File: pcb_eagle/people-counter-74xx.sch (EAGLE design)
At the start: 66 parts, among them IC1 74LS90N, IC2 74LS90N, IC3 74LS90N, IC4 74LS90N, IC5 74LS47N, IC6 74LS47N, IC7 74LS47N, IC8 74LS47N, IC9 NE555N, X1 USB-MICRO-B-BOTTOM

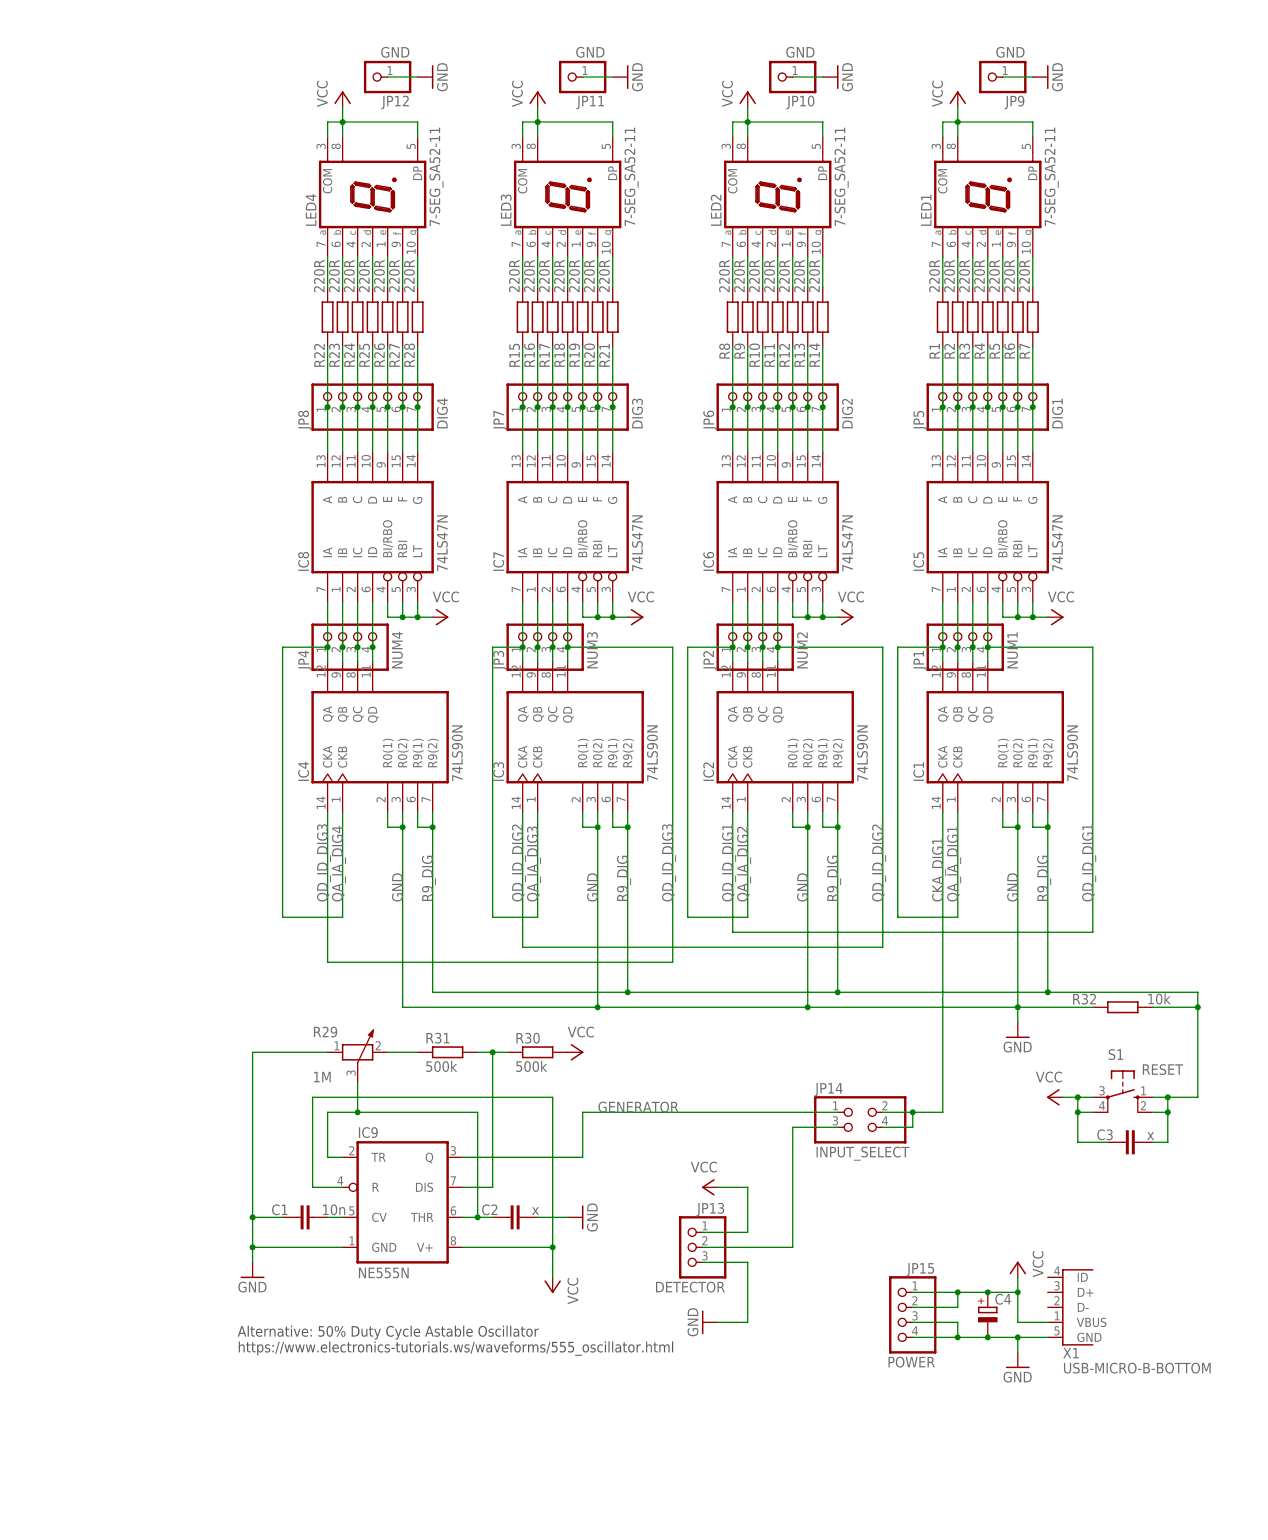
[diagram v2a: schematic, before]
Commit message: PCB_EAGLE: final layout of board
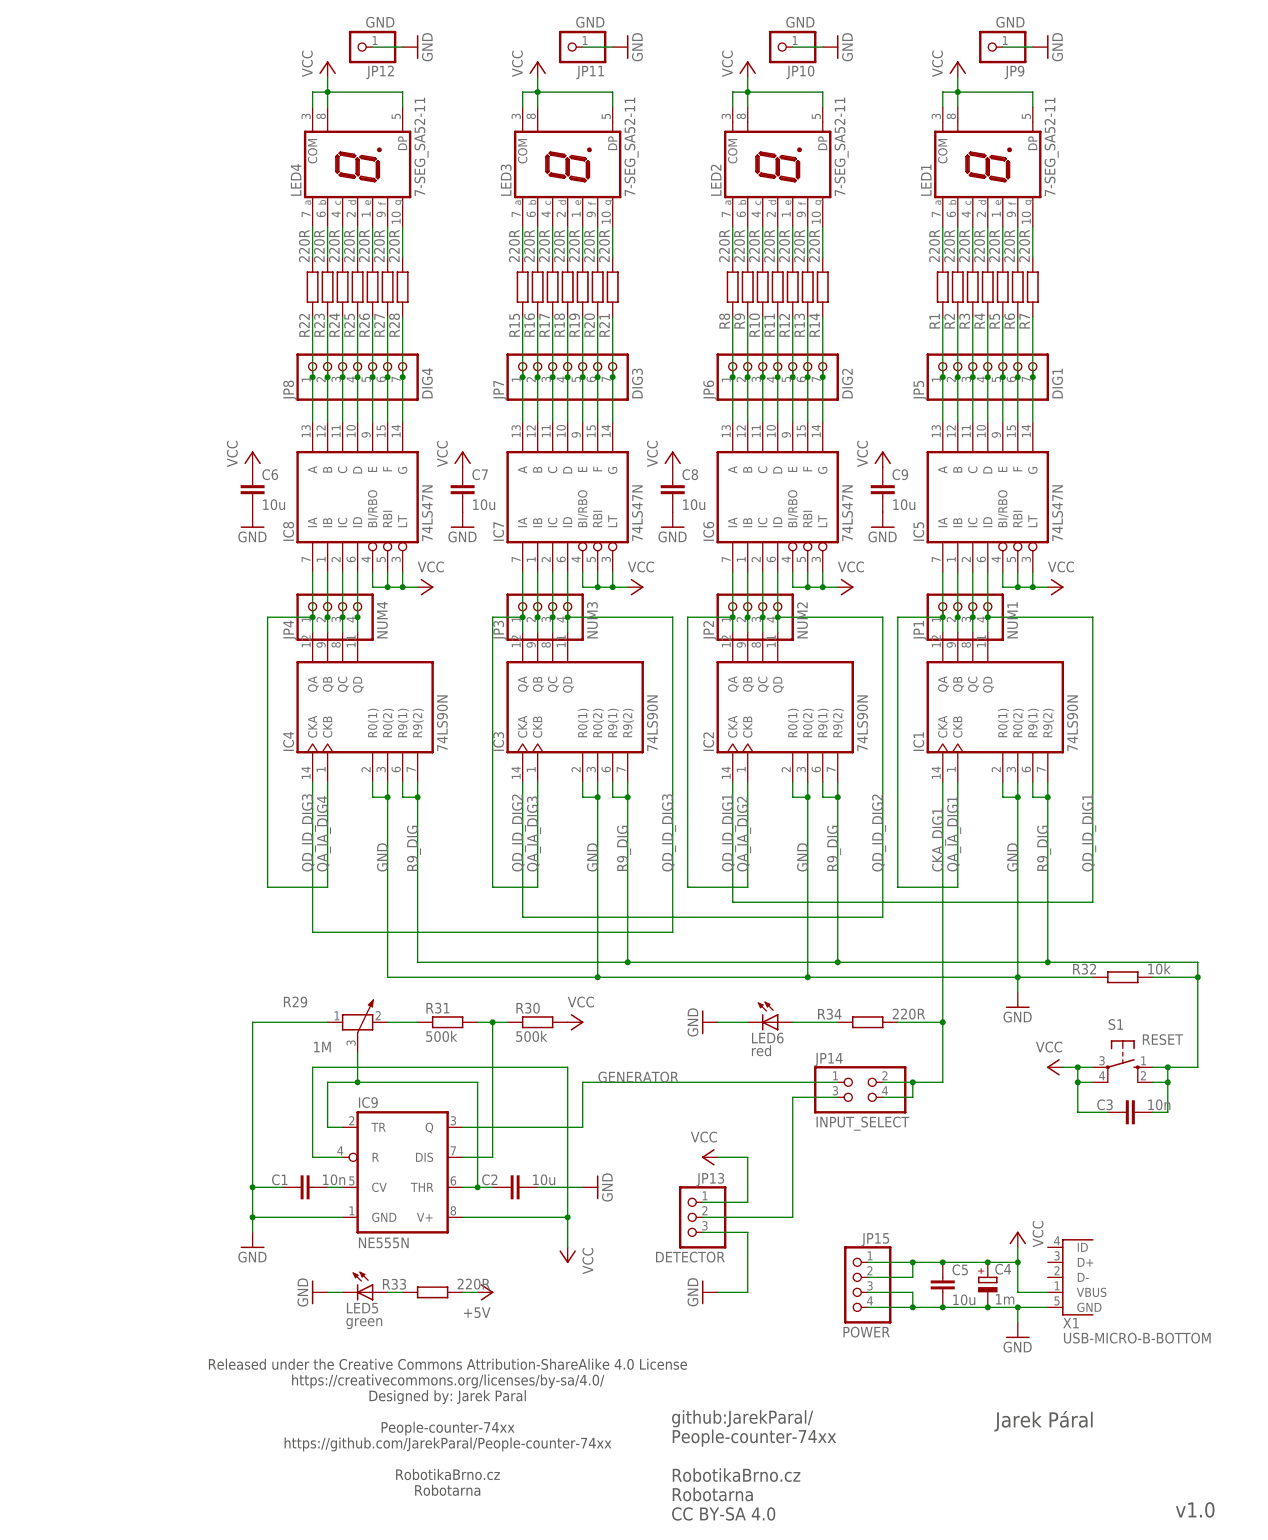
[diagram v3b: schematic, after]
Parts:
- added C5, C6, C7, C8, C9: 10u, rcl:C-EUC0805
- added LED5: green, led:LEDCHIPLED_0603
- added LED6: red, led:LEDCHIPLED_0603
- added R33, R34: 220R, rcl:R-EU_R0603
- C2: value x -> 10u; device rcl:C-EUC0603 -> rcl:C-EUC0805
- C3: value x -> 10n
- C4: value (none) -> 1m
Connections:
- new net +5V: R33.2
- new net N$1: LED6.A, R34.1
- new net N$11: LED5.A, R33.1
- net CKA_DIG1: now also R34.2
- net GND: now also C5.2, C6.2, C7.2, C8.2, C9.2, LED5.C, LED6.C
- net VCC: now also C5.1, C6.1, C7.1, C8.1, C9.1
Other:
- note added: "Jarek Páral"
- note added: "Released under the Creative Commons Attribution-ShareAlike 4.0 License https://creativecommons.org/licenses/by-sa/4.0/ Designed by: Jarek Paral People-counter-74xx https://github.com/JarekParal/People-counter-74xx RobotikaBrno.cz Robotarna"
- note added: "github:JarekParal/ People-counter-74xx RobotikaBrno.cz Robotarna CC BY-SA 4.0"
- note added: "v1.0"
- note removed: "Alternative: 50% Duty Cycle Astable Oscillator https://www.electronics-tutorials.ws/waveforms/555_oscillator.html"
- moved on the sheet: C1, C2, C3, C4, IC1, IC2, IC3, IC4, IC5, IC6, IC7, IC8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

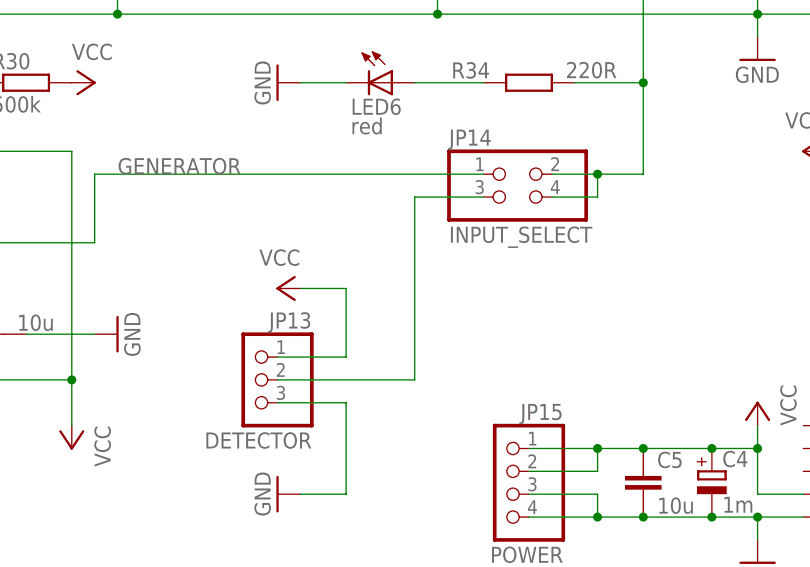
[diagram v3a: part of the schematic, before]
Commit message: PCB_EAGLE: add a few description text and some optimization of net
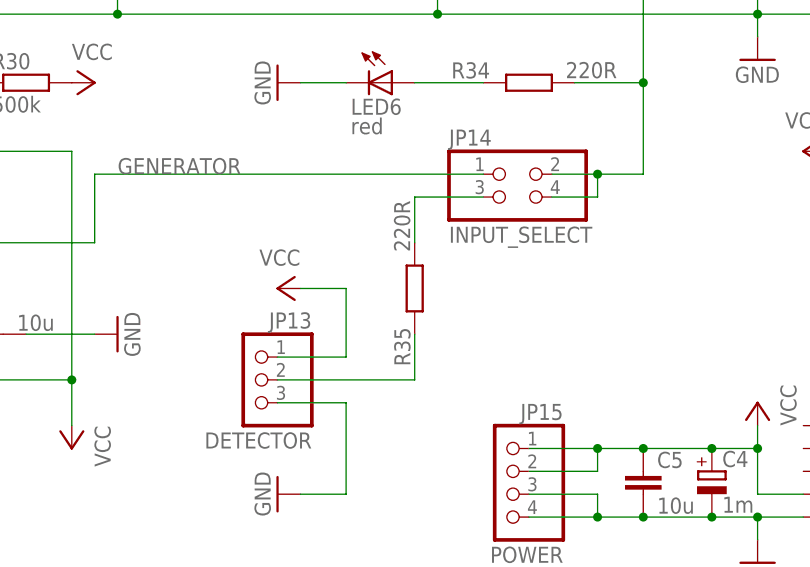
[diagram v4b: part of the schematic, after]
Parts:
- added R35: 220R, rcl:R-EU_R0603
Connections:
- removed net N$5: JP13.2, JP14.3
- new net SIGNAL_INPUT: JP13.2, R35.1
- new net SIGNAL_INPUT_: JP14.3, R35.2
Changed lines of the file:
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@@
 <part name="GND15" library="supply1" deviceset="GND" device=""/>
 <part name="R34" library="rcl" library_urn="urn:adsk.eagle:library:334" deviceset="R-EU_" device="R0603" package3d_urn="urn:adsk.eagle:package:23555/2" value="220R"/>
+<part name="R35" library="rcl" library_urn="urn:adsk.eagle:library:334" deviceset="R-EU_" device="R0603" package3d_urn="urn:adsk.eagle:package:23555/2" value="220R"/>
 </parts>
 <sheets>
@@
 <attribute name="VALUE" x="100.584" y="-73.152" size="1.778" layer="96"/>
 </instance>
+<instance part="R35" gate="G$1" x="83.82" y="-96.52" smashed="yes" rot="R90">
+<attribute name="NAME" x="83.3374" y="-100.838" size="1.778" layer="95" rot="MR270"/>
+<attribute name="VALUE" x="83.312" y="-92.456" size="1.778" layer="96" rot="R90"/>
+</instance>
 </instances>
 <busses>
@@
 </segment>
 </net>
-<net name="N$5" class="0">
+<net name="SIGNAL_INPUT" class="0">
 <segment>
 <pinref part="JP13" gate="A" pin="2"/>
 <wire x1="68.58" y1="-106.68" x2="83.82" y2="-106.68" width="0.1524" layer="91"/>
-<wire x1="83.82" y1="-106.68" x2="83.82" y2="-86.36" width="0.1524" layer="91"/>
-<pinref part="JP14" gate="A" pin="3"/>
-<wire x1="83.82" y1="-86.36" x2="91.44" y2="-86.36" width="0.1524" layer="91"/>
+<pinref part="R35" gate="G$1" pin="1"/>
+<wire x1="83.82" y1="-101.6" x2="83.82" y2="-106.68" width="0.1524" layer="91"/>
 </segment>
 </net>
@@
 </segment>
 </net>
+<net name="SIGNAL_INPUT_" class="0">
+<segment>
+<pinref part="JP14" gate="A" pin="3"/>
+<wire x1="83.82" y1="-86.36" x2="91.44" y2="-86.36" width="0.1524" layer="91"/>
+<pinref part="R35" gate="G$1" pin="2"/>
+<wire x1="83.82" y1="-91.44" x2="83.82" y2="-86.36" width="0.1524" layer="91"/>
+</segment>
+</net>

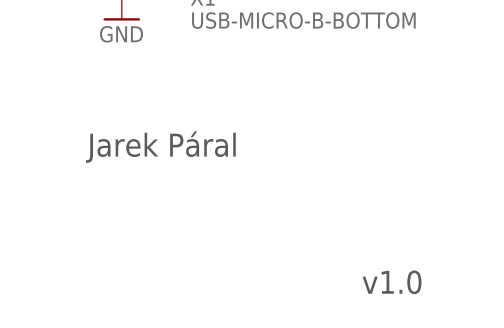
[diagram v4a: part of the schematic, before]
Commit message: PCB_EAGLE: start work on version 1.1 - repair layer of texts Robotarna RobotikaBrno
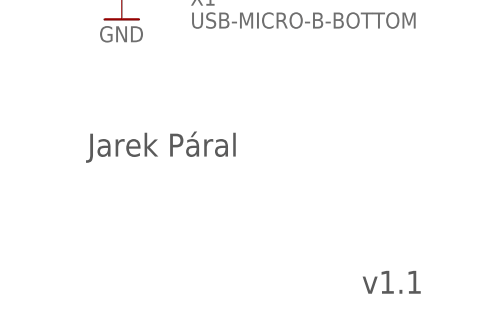
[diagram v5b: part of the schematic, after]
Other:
- note added: "v1.1"
- note removed: "v1.0"
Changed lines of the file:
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@@
 CC BY-SA 4.0</text>
 <text x="118.11" y="-142.24" size="2.54" layer="97" font="vector" ratio="14">Jarek Páral</text>
-<text x="148.59" y="-157.48" size="2.54" layer="97" font="vector" ratio="14">v1.0</text>
+<text x="148.59" y="-157.48" size="2.54" layer="97" font="vector" ratio="14">v1.1</text>
 <rectangle x1="511.290040625" y1="-62.8899625" x2="511.503396875" y2="-62.8798" layer="102"/>
 <rectangle x1="511.1478" y1="-62.8798" x2="511.6456375" y2="-62.86964375" layer="102"/>

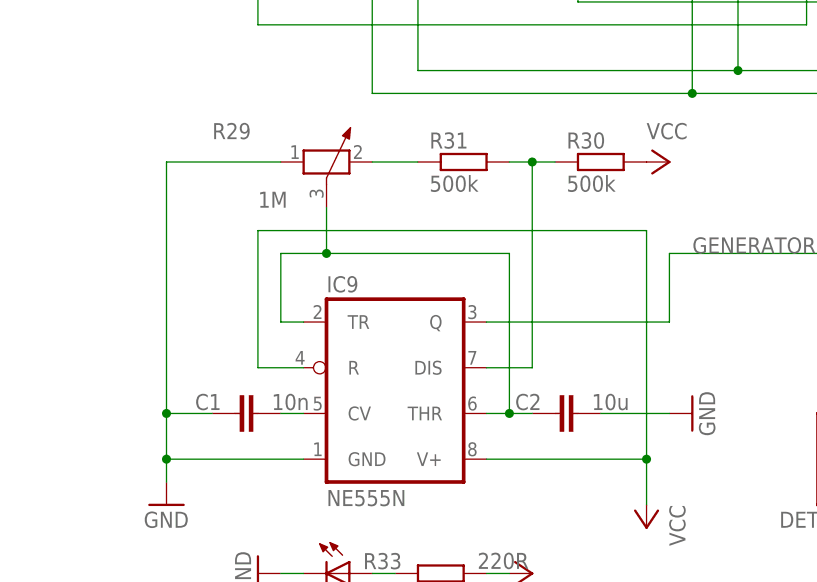
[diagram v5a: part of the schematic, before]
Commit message: PCB_EAGLE: fix two bugs from v1.0 - change value of C2 (10u -> 200n) - delete one wire on potentiometer (R29)
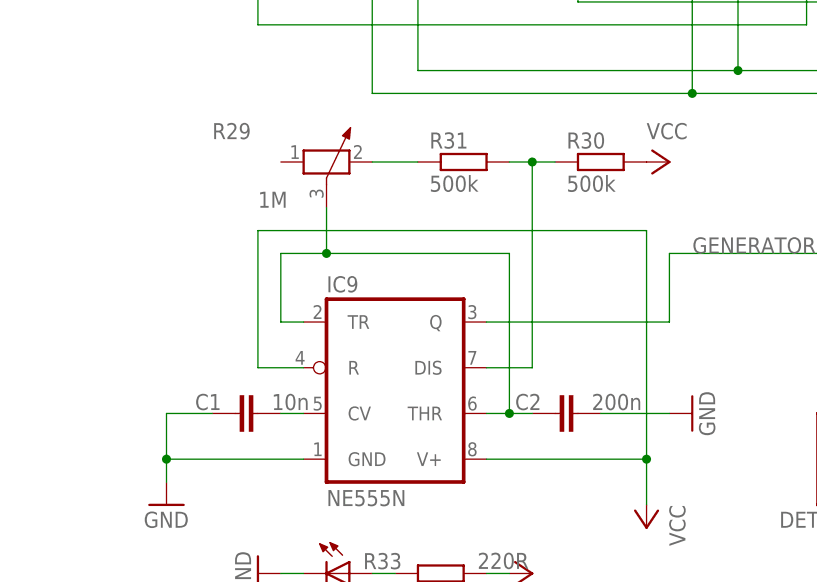
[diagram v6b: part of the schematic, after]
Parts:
- C2: value 10u -> 200n
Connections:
- net GND: no longer R29.1
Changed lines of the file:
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@@
 <?xml version="1.0" encoding="utf-8"?>
 <!DOCTYPE eagle SYSTEM "eagle.dtd">
-<eagle version="8.6.0">
+<eagle version="9.1.2">
 <drawing>
 <settings>
@@
 <part name="JP13" library="pinhead" library_urn="urn:adsk.eagle:library:325" deviceset="PINHD-1X3" device="/90" package3d_urn="urn:adsk.eagle:package:22459/2" value="DETECTOR"/>
 <part name="R32" library="rcl" library_urn="urn:adsk.eagle:library:334" deviceset="R-EU_" device="R0603" package3d_urn="urn:adsk.eagle:package:23555/2" value="10k"/>
-<part name="C2" library="rcl" library_urn="urn:adsk.eagle:library:334" deviceset="C-EU" device="C0805" package3d_urn="urn:adsk.eagle:package:23617/2" value="10u"/>
+<part name="C2" library="rcl" library_urn="urn:adsk.eagle:library:334" deviceset="C-EU" device="C0805" package3d_urn="urn:adsk.eagle:package:23617/2" value="200n"/>
 <part name="C3" library="rcl" library_urn="urn:adsk.eagle:library:334" deviceset="C-EU" device="C0603" package3d_urn="urn:adsk.eagle:package:23616/2" value="10n"/>
 <part name="GND1" library="supply1" library_urn="urn:adsk.eagle:library:371" deviceset="GND" device=""/>
@@
 <pinref part="C1" gate="G$1" pin="1"/>
 <wire x1="-7.62" y1="-101.6" x2="-2.54" y2="-101.6" width="0.1524" layer="91"/>
-<pinref part="R29" gate="1" pin="1"/>
-<wire x1="5.08" y1="-73.66" x2="-7.62" y2="-73.66" width="0.1524" layer="91"/>
-<wire x1="-7.62" y1="-73.66" x2="-7.62" y2="-101.6" width="0.1524" layer="91"/>
-<junction x="-7.62" y="-101.6"/>
-</segment>
-<segment>
+</segment>
+<segment>
